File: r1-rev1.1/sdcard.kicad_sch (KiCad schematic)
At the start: 6 parts, among them J3 TF-115

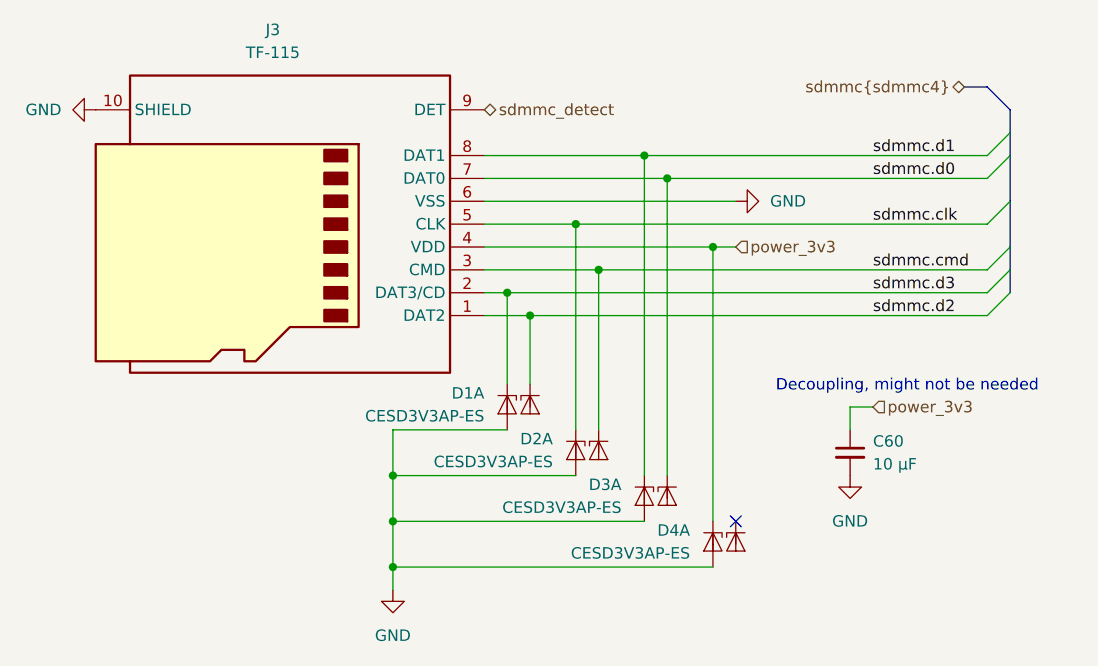
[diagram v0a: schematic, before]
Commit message: R1-Rev1.1: remove SDMMC ESD diodes and adjust routing
Remove the CESD3V3-AP ESD diodes and put a TODO to select
new diodes later. While here, reroute the SDMMC bus a bit
so it's not so messy.

See Github issue: #27
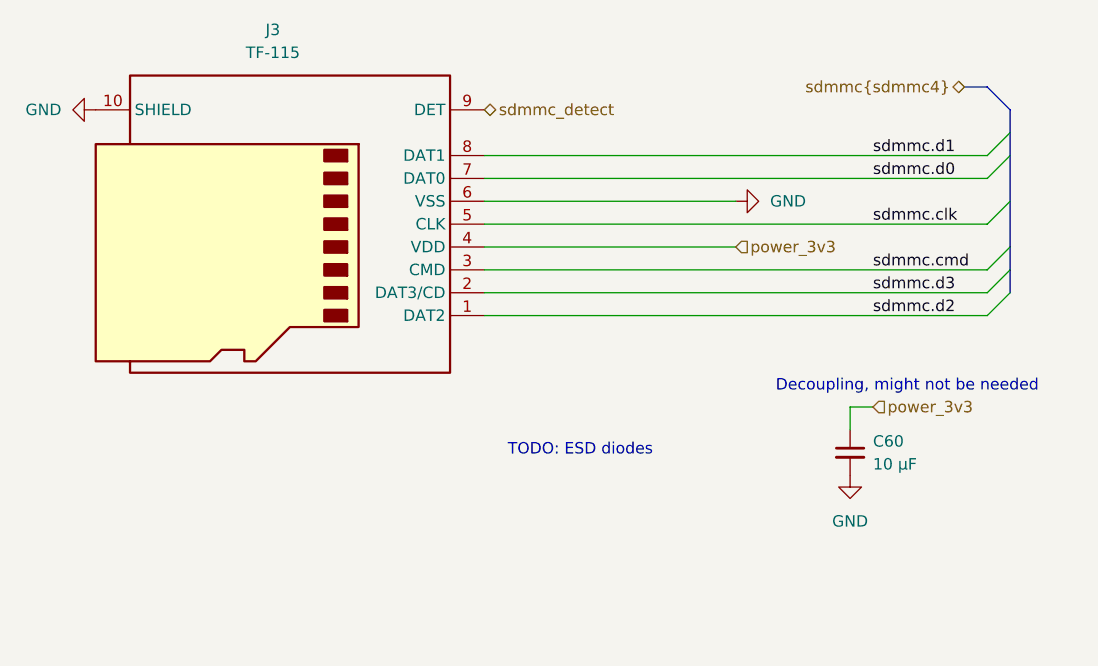
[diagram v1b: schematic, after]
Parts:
- removed D1, D2, D3, D4: CESD3V3AP-ES, Package_TO_SOT_SMD:SOT-23, symbol echoplayer:CESD3V3AP-ES
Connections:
- no-connect marks 1 -> 0
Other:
- note added: "TODO: ESD diodes"
